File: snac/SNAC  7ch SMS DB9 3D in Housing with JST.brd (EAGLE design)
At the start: 61.2 x 64.2 mm, 46 parts, among them IC1 4030D, IC2 MAX660CPACS, Q1 BSS138, Q2 BSS138, Q3 BSS138, Q4 BSS138, Q5 BSS138, Q6 BSS138, Q7 BSS138, Q8 BSS138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

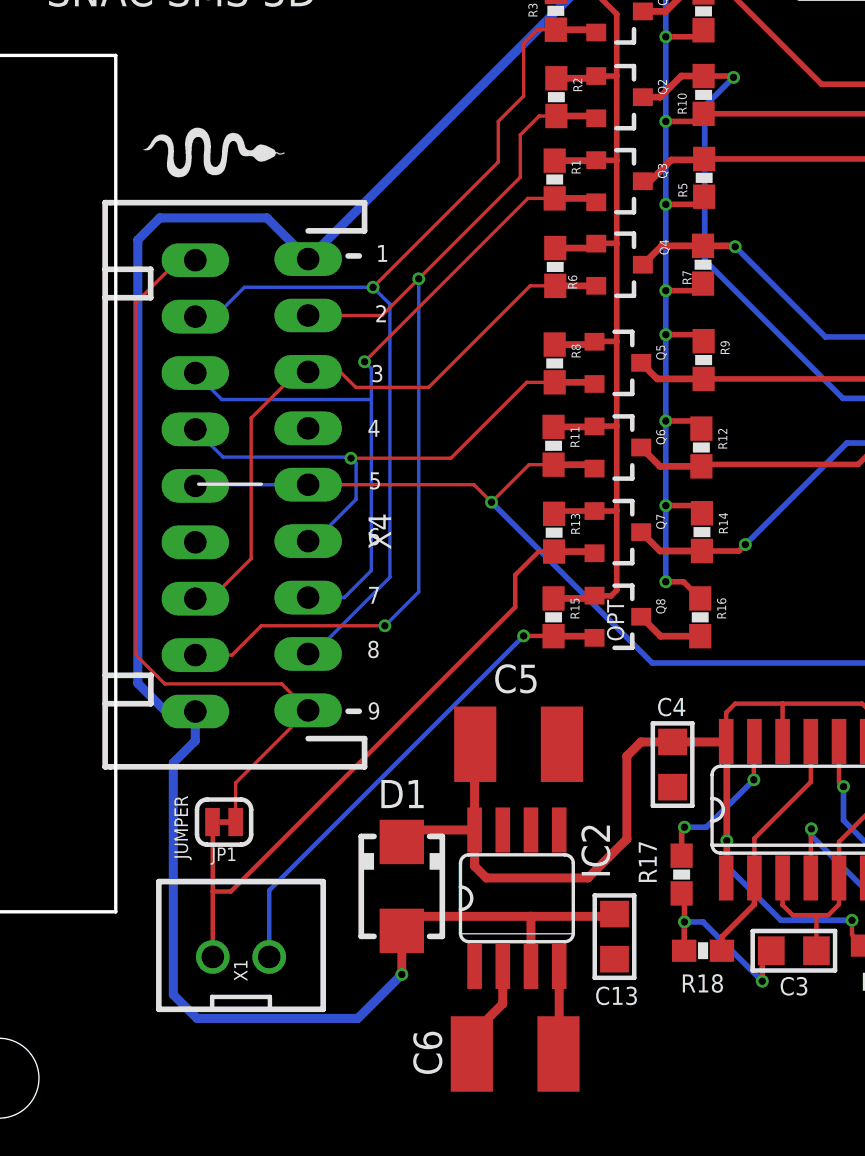
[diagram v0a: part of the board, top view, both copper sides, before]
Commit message: fixed major screw-up with the USERIO/JST pinout. Removed the unused FET
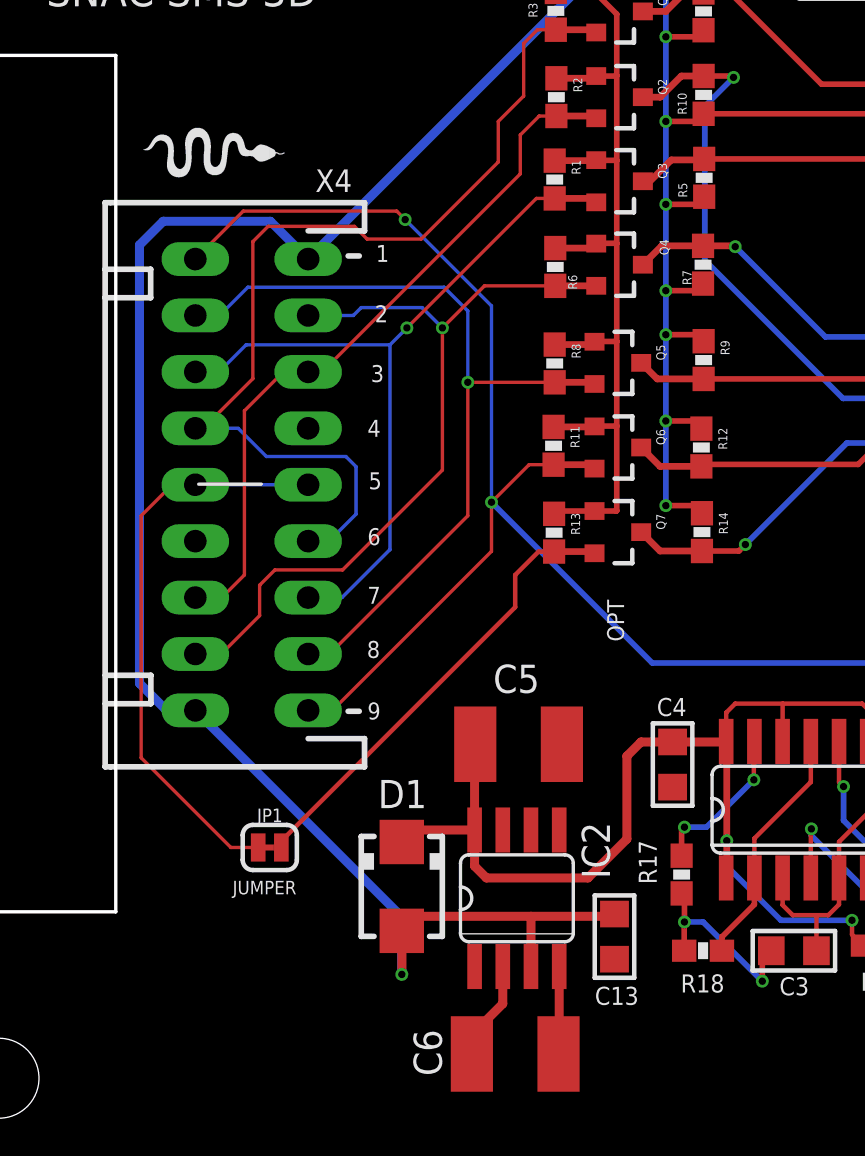
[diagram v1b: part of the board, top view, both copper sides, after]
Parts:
- removed Q8: BSS138, SparkFun:SOT23-3
- removed R15, R16: 10K, SparkFun:0603-RES
- removed X1: JST-XH-02-PIN-ROUND-PAD, Rembrandt Electronics - JST XH Connectors v1-0:JST-XH-02-PACKAGE-ROUND-PAD
- U1: value PMIC-LDO-XC6206P332MR-G(SOT23) -> AP2127N-3.3TRG1
- moved JP1 2.35 mm to (16.4, 15.8), turned to 0 degrees
- moved X5 0.05 mm to (13.0, 32.2)
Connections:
- removed net HV8: Q8.3, R16.2
- removed net LV8: Q8.2, R15.2, X1.2
- net HV: no longer R16.1
- net J1: now also X4.5, X5.5; no longer X4.9, X5.9
- net LV: no longer Q8.1, R15.1
- net LV1: now also X4.6, X5.6; no longer X4.8, X5.8
- net LV2: now also X4.3, X5.3; no longer X4.2, X5.2
- net LV4: now also X4.2, X5.2; no longer X4.3, X5.3
- net LV5: now also X4.8, X5.8; no longer X4.6, X5.6
- net LV6: now also X4.9, X5.9; no longer X4.5, X5.5
- net LV7: no longer X1.1
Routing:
- net LV6: track 47.0 -> 71.6 mm, vias 2 -> 3
- net LV8: track 22.6 -> 0.00 mm, vias 1 -> 0
- net HV: track 154.5 -> 139.8 mm, vias 10 -> 9
- net LV5: track 25.0 -> 38.2 mm
- net LV2: track 43.2 -> 32.4 mm, vias 2 -> 0
- net LV7: track 30.5 -> 20.7 mm
- net J1: track 34.5 -> 25.9 mm
- net LV4: track 28.2 -> 36.1 mm, vias 0 -> 1
- net LV: track 54.5 -> 47.9 mm
- net HV8: track 3.02 -> 0.00 mm
- net LV1: track 44.4 -> 44.8 mm, vias 1 -> 0

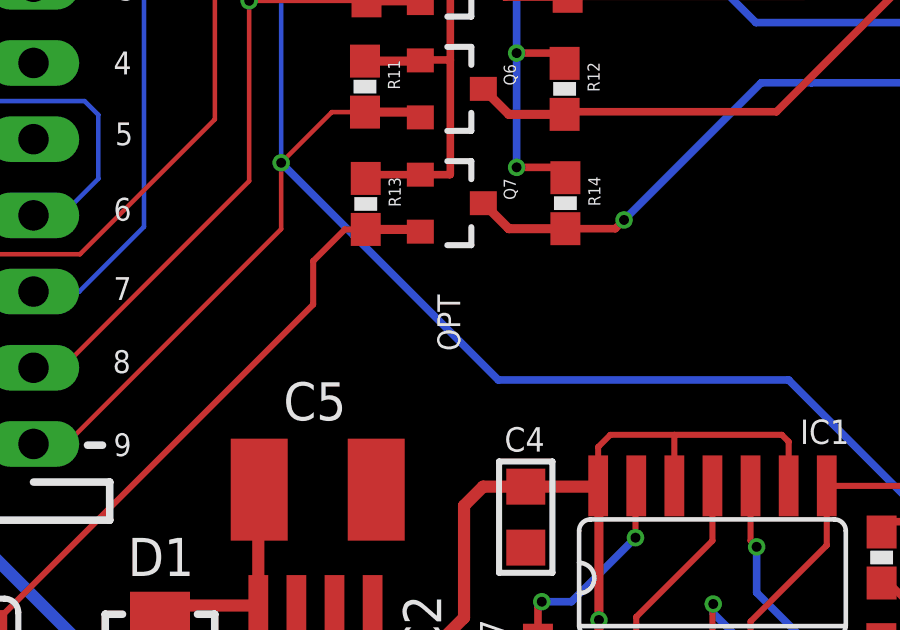
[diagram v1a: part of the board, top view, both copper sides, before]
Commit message: slight tidy of SMS DB9 3D board
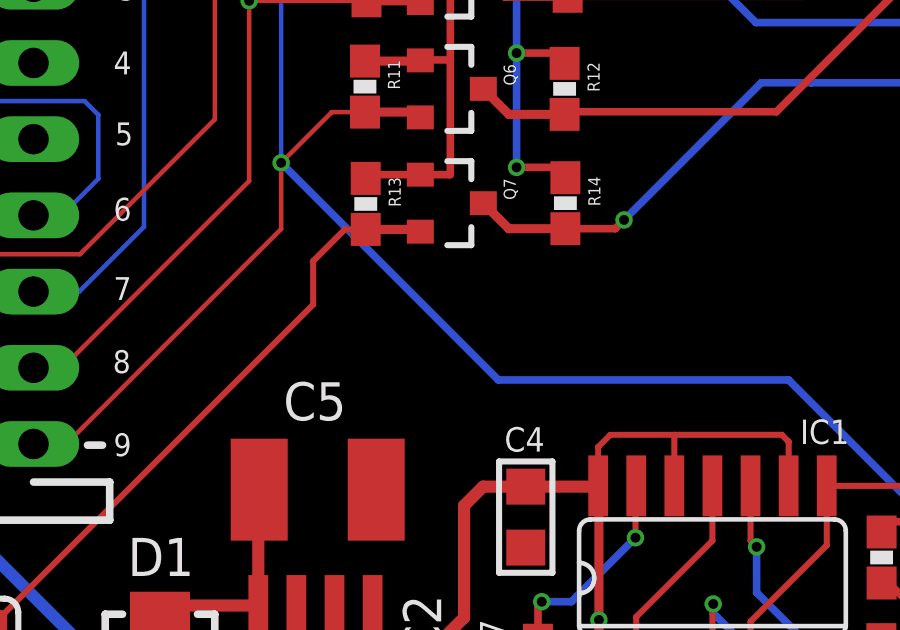
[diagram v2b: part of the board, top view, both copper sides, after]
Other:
- board text removed: "OPT"
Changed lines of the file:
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@@
 <rectangle x1="13.421359375" y1="58.059321875" x2="13.502640625" y2="58.069478125" layer="21"/>
 <text x="9.1694" y="60.8838" size="0.8128" layer="16" font="vector" ratio="22" rot="MR180">V02</text>
-<text x="32.3342" y="25.1206" size="0.762" layer="21" font="vector" ratio="15" rot="R90">OPT</text>
 <text x="32.639" y="58.3692" size="0.6096" layer="21" font="vector" ratio="15">1uf</text>
 <text x="26.3652" y="54.7116" size="0.6096" layer="21" font="vector" ratio="15" rot="R180">1uf</text>

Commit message: LV6/LV7 selection jumper added to SMS 3D board
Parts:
- added JP2: (no value), jumper:JP2
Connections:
- new net N$27: JP2.2, R20.1
- net LV6: now also JP2.1; no longer R20.1
- net LV7: now also JP2.3
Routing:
- net N$27: track 0.00 -> 38.0 mm, vias 0 -> 1
- net LV6: track 71.6 -> 63.5 mm
- net LV7: track 20.7 -> 25.3 mm
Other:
- board text added: "LV6"
- board text added: "LV7"
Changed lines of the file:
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@@
 <wire x1="9.4488" y1="51.5112" x2="1.0668" y2="51.5112" width="0.1524" layer="20"/>
 <wire x1="1.0668" y1="51.5112" x2="1.0668" y2="65.3034" width="0.1524" layer="20"/>
+<text x="12.573" y="5.715" size="1.016" layer="21">LV6</text>
+<text x="12.6492" y="10.8204" size="1.016" layer="21">LV7</text>
 </plain>
 <attributes>
@@
 <attribute name="VALUE" x="34.8742" y="10.0584" size="0.4064" layer="27" font="vector"/>
 </element>
+<element name="JP2" library="jumper" package="JP2" value="" x="16.9164" y="8.6868" smashed="yes" rot="R90">
+<attribute name="NAME" x="15.3416" y="3.0226" size="1.27" layer="25" ratio="10"/>
+<attribute name="VALUE" x="21.2344" y="5.1308" size="1.27" layer="27" ratio="10" rot="R90"/>
+</element>
 </elements>
 <signals>
@@
 <wire x1="30.816" y1="33.0962" x2="30.8042" y2="33.0844" width="0.1778" layer="1"/>
 <wire x1="30.8042" y1="33.0844" x2="29.1592" y2="33.0844" width="0.3048" layer="1"/>
-<contactref element="R20" pad="1"/>
-<wire x1="46.3804" y1="19.0872" x2="46.7242" y2="19.431" width="0.254" layer="1"/>
-<wire x1="46.7242" y1="19.431" x2="47.5488" y2="19.431" width="0.254" layer="1"/>
-<wire x1="47.5488" y1="19.431" x2="47.7774" y2="19.6596" width="0.254" layer="1"/>
-<via x="47.7774" y="19.6596" extent="1-16" drill="0.3302"/>
 <wire x1="29.1592" y1="33.0844" x2="28.0552" y2="33.0844" width="0.1524" layer="1"/>
 <via x="26.3652" y="31.3944" extent="1-16" drill="0.3302"/>
-<wire x1="26.3652" y1="31.3944" x2="33.6042" y2="24.1554" width="0.254" layer="16"/>
 <wire x1="28.0552" y1="33.0844" x2="26.3652" y2="31.3944" width="0.1524" layer="1"/>
-<wire x1="33.6042" y1="24.1554" x2="43.2816" y2="24.1554" width="0.254" layer="16"/>
-<wire x1="43.2816" y1="24.1554" x2="47.7774" y2="19.6596" width="0.254" layer="16"/>
 <contactref element="X4" pad="9"/>
 <contactref element="X5" pad="9"/>
@@
 <wire x1="22.098" y1="44.5008" x2="15.1892" y2="44.5008" width="0.1524" layer="1"/>
 <wire x1="15.1892" y1="44.5008" x2="13.0302" y2="42.3418" width="0.1524" layer="1"/>
+<contactref element="JP2" pad="1"/>
+<wire x1="16.9164" y1="6.1468" x2="15.0368" y2="6.1468" width="0.2032" layer="16"/>
+<wire x1="15.0368" y1="6.1468" x2="14.097" y2="7.0866" width="0.2032" layer="16"/>
+<wire x1="14.097" y1="7.0866" x2="14.097" y2="17.8308" width="0.2032" layer="16"/>
+<wire x1="14.097" y1="17.8308" x2="14.478" y2="18.2118" width="0.2032" layer="16"/>
+<via x="14.478" y="18.2118" extent="1-16" drill="0.35"/>
+<wire x1="14.478" y1="18.2118" x2="14.478" y2="18.3896" width="0.2032" layer="1"/>
+<wire x1="14.478" y1="18.3896" x2="18.1102" y2="22.0218" width="0.2032" layer="1"/>
 </signal>
 <signal name="HV6">
@@
 <wire x1="27.432" y1="26.67" x2="16.891" y2="16.129" width="0.2032" layer="1"/>
 <wire x1="16.891" y1="16.129" x2="16.891" y2="15.8623" width="0.2032" layer="1"/>
+<contactref element="JP2" pad="3"/>
+<wire x1="16.9037" y1="15.8496" x2="16.9037" y2="11.2395" width="0.2032" layer="1"/>
+<wire x1="16.9037" y1="11.2395" x2="16.9164" y2="11.2268" width="0.2032" layer="1"/>
 </signal>
 <signal name="HV7">
@@
 <wire x1="35.052" y1="13.6534" x2="35.052" y2="12.4968" width="0.254" layer="1"/>
 </signal>
+<signal name="N$27">
+<contactref element="JP2" pad="2"/>
+<contactref element="R20" pad="1"/>
+<wire x1="46.3804" y1="19.0872" x2="47.029" y2="19.7358" width="0.2032" layer="1"/>
+<wire x1="47.029" y1="19.7358" x2="47.625" y2="19.7358" width="0.2032" layer="1"/>
+<via x="47.625" y="19.7358" extent="1-16" drill="0.35"/>
+<wire x1="47.625" y1="19.7358" x2="46.1772" y2="21.1836" width="0.2032" layer="16"/>
+<wire x1="46.1772" y1="21.1836" x2="36.8046" y2="21.1836" width="0.2032" layer="16"/>
+<wire x1="36.8046" y1="21.1836" x2="24.3078" y2="8.6868" width="0.2032" layer="16"/>
+<wire x1="24.3078" y1="8.6868" x2="16.9164" y2="8.6868" width="0.2032" layer="16"/>
+</signal>
 </signals>
